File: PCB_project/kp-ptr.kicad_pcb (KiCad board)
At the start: 4 copper layers, 25 x 74 mm, 140 parts, among them IC1 TPS62142, J1 ESP32_PROG_CON, J10 Conn_01x02, J11 Conn_01x02, J12 Conn_01x02, J14 Molex 104031-0811, J2 Conn_01x02, J3 Conn_02x02_Odd_Even, J4 USB_C_Receptacle_USB2.0, J7 Conn_01x02_Male, J8 BM06B-GHS-TBT(LF)(SN), Q1 AO3400A, Q12 AO3400A, Q2 AO3401A, Q4 AO3401A, Q6 AO3400A, Q7 AO3400A, Q8 AO3401A, U1 ESP32-S3FN8, U10 AMS1117-3.3, U11 USBLC6-2SC6-ES, U13 W25Q256, U2 MS560702BA03-50, U3 H3LIS331, U4 LSM6DSV32, Y1 7M40000005-40MHz

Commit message: Missing pullup on BOOT pin fixed. Some cleanup
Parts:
- added R20: 10k, Resistor_SMD:R_0402_1005Metric, B.Cu at (18.0, 32.7)
- D10, D11, D12, D13: value SMT_12B-2020_WDS -> WS2812B-2020
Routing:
- net IO0: track 14.4 -> 14.9 mm
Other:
- board text added: "3V3"
- board text removed: "NC"

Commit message: + USB connector changed to SMD
+ igniters connectors changed to single 6 pin connector
+ buzzer selected
+ crystal changed to TCXO (experimental)
+ JLC production files generated
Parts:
- removed C10, C9: 12p, Capacitor_SMD:C_0402_1005Metric
- removed J10, J11, J12: Conn_01x02, TerminalBlock_4Ucon:TerminalBlock_4Ucon_1x02_P3.50mm_Horizontal
- removed L3: 24nH, Inductor_SMD:L_0402_1005Metric
- removed Y1: 7M40000005-40MHz, KP-PTR_lib:XTAL_TSX-3225_16.0000MF18X-AC3
- added C24: 100nF, Capacitor_SMD:C_0402_1005Metric, B.Cu at (12.4, 21.3)
- added C25: 10nF, Capacitor_SMD:C_0402_1005Metric, B.Cu at (13.9, 24.4)
- added C26: 10nF, Capacitor_SMD:C_0402_1005Metric, B.Cu at (13.9, 23.4)
- added J5: DB125-3.5-6P-GN-S, TerminalBlock_Phoenix:TerminalBlock_Phoenix_PT-1,5-6-3.5-H_1x06_P3.50mm_Horizontal, F.Cu at (18.1, 58.4)
- added R44: 1k, Resistor_SMD:R_0402_1005Metric, B.Cu at (6.92, 37.8)
- added Y2: X1G0054210307, Oscillator:Oscillator_SMD_SeikoEpson_TG2520SMN-xxx-xxxxxx-4Pin_2.5x2.0mm, B.Cu at (14.6, 21.5)
- C11, C13, C6: value 1u -> 1uF
- C12, C39: value 10n -> 10nF
- C14, C15, C3, C7, C8: value 100n -> 100nF
- C18, C21, C41, C66: footprint Capacitor_SMD:C_0402_1005Metric -> Capacitor_SMD:C_0603_1608Metric
- C40: value 100n 16V -> 100nF 16V
- C45: value 470pF -> 10nF
- C5: value 10u -> 10uF; footprint Capacitor_SMD:C_0402_1005Metric -> Capacitor_SMD:C_0603_1608Metric
- J3: value Conn_02x02_Odd_Even -> 67996-104HLF
- J4: value USB_C_Receptacle_USB2.0 -> USB4105-GF-A-120; footprint KP-PTR_lib:USB_C_213716 -> KP-PTR_lib:USB_C_16P_SMD_USB4105-GF-A
- LS1: value CBT-09427-SMT -> GMD0955YB-3V2700
- U10: value AMS1117-3.3 -> AMS1117-5.0
- moved C21 2.74 mm to (4.90, -0.10)
- moved J4 1.20 mm to (3.80, 8.17)
- moved C55 0.98 mm to (12.8, 56.4)
- moved R81 0.95 mm to (0.83, 6.06)
- moved R84 0.95 mm to (0.83, 5.25)
- moved C56 0.91 mm to (12.8, 49.4)
- moved C57 0.85 mm to (12.8, 42.3)
- moved R54 0.72 mm to (12.7, 46.8)
- moved R67 0.68 mm to (12.8, 39.9)
- moved R53 0.65 mm to (12.7, 53.8)
- moved Q4 0.55 mm to (15.1, 48.0)
- moved Q8 0.55 mm to (15.1, 41.0)
- moved Q2 0.55 mm to (15.1, 55.0)
- moved C18 0.50 mm to (6.50, 5.86)
- moved C5 0.46 mm to (16.6, 29.5)
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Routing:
- net Earth: track 59.1 -> 49.8 mm, vias 91 -> 93
- net Net-(J4-CC1): track 12.5 -> 4.54 mm
- net VCC: track 47.3 -> 54.8 mm, vias 10 -> 7
- net Net-(U1-XTAL_N): track 11.2 -> 4.16 mm
- net +3V3: track 86.2 -> 92.3 mm, vias 31 -> 34
- net VBUS: track 46.7 -> 42.6 mm
- net Net-(Y2-OUT): track 0.00 -> 3.19 mm
- net Net-(C9-Pad2): track 2.89 -> 0.00 mm
- net Net-(D14-A): track 5.80 -> 7.32 mm
- net Net-(U1-XTAL_P): track 4.51 -> 3.32 mm
- net Net-(J4-D+-PadA6): track 4.20 -> 5.20 mm, vias 0 -> 1
- net USB_DM: track 29.1 -> 29.9 mm
- net IGN2_DET: track 25.8 -> 26.7 mm
- net USB_DP: track 29.0 -> 29.8 mm
- net Net-(J4-CC2): track 3.07 -> 3.21 mm, vias 0 -> 1
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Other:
- board text added: "+VCC-"
- board text added: "<13V"
- board text removed: "+BAT-"
- board text removed: "max 13V"

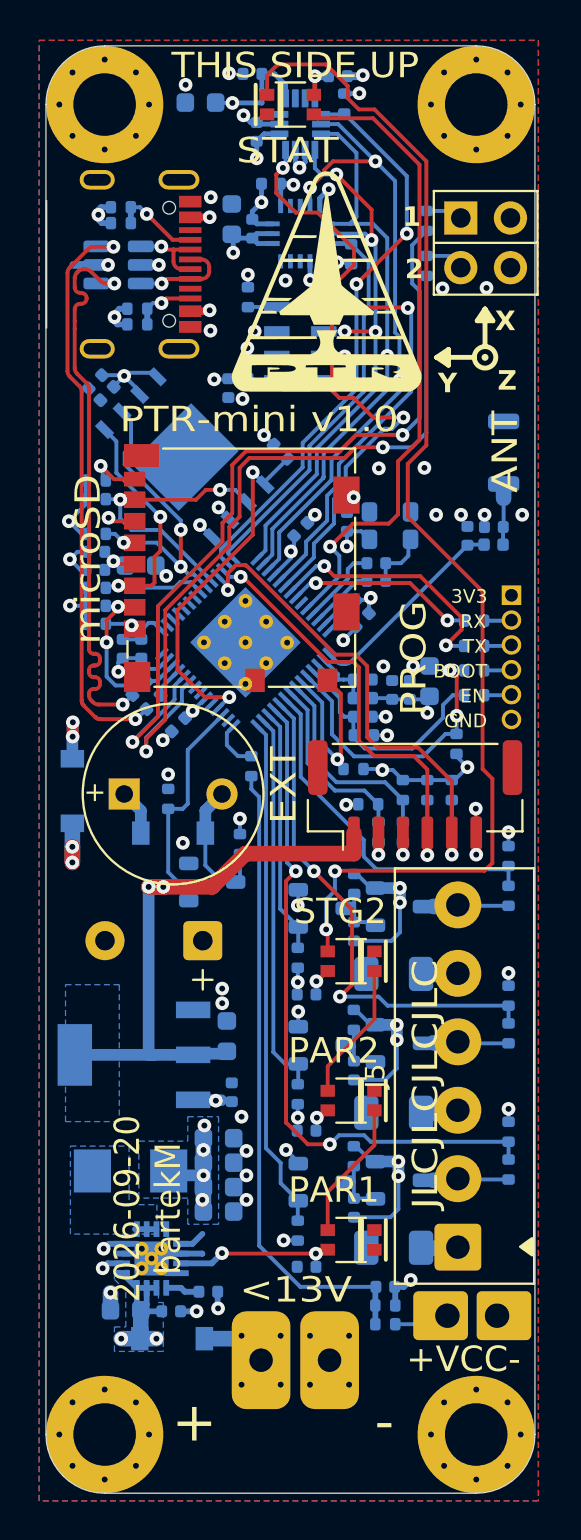
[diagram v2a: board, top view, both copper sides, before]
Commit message: + LDO replaced with better one (lower voltage drop)
+ Vbat meas circuit should be now more stable
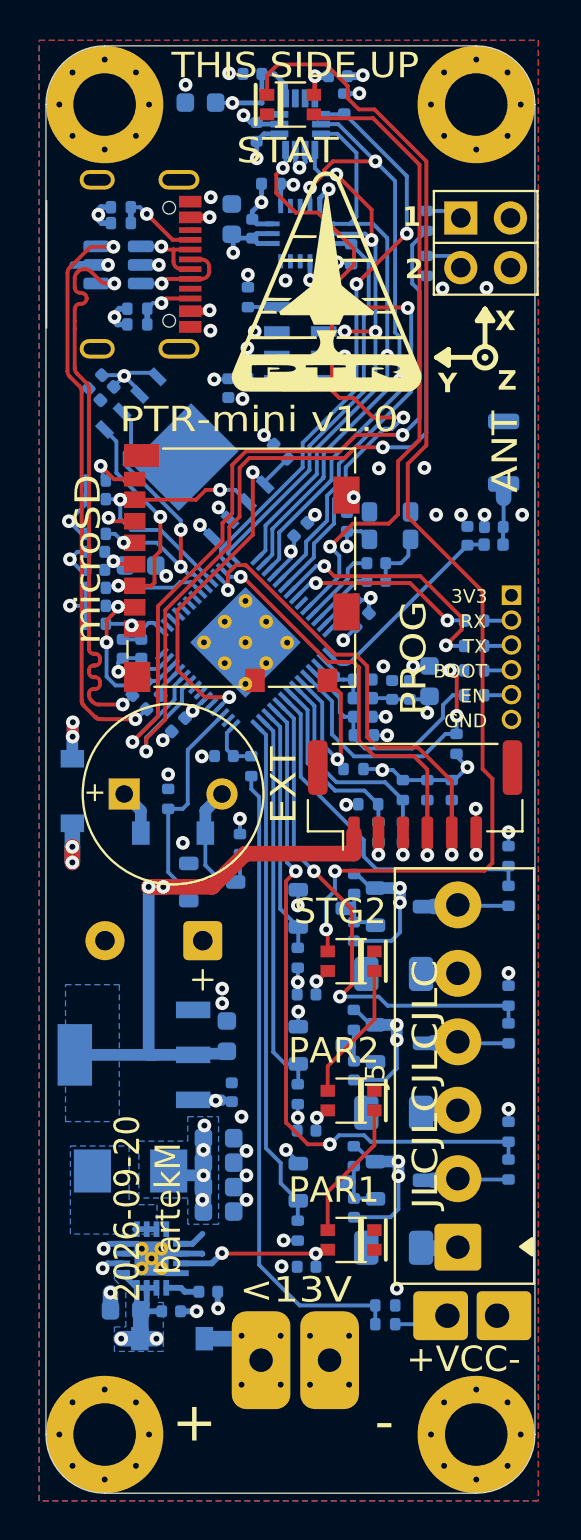
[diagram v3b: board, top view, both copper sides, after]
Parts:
- C39: value 10nF -> 1uF
- R32: value 10k -> 22R
- U10: value AMS1117-5.0 -> LDL1117S50R
- moved C39 28.4 mm to (6.10, 33.3), turned to 180 degrees
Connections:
- C39 pad 1: Net-(C39-Pad1) -> VBAT_MEAS
- R31 pad 2: Net-(C39-Pad1) -> Net-(R31-Pad2)
- R32 pad 1: Net-(C39-Pad1) -> Net-(R31-Pad2)
- R33 pad 1: Net-(C39-Pad1) -> Net-(R31-Pad2)
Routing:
- net Net-(C39-Pad1): track 32.9 -> 0.00 mm
- net Net-(R31-Pad2): track 0.00 -> 32.9 mm
- net Earth: track 49.8 -> 47.8 mm, vias 93 -> 95
